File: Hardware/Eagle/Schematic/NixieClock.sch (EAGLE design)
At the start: 12 parts, among them X1 5566-12, X7 5566-12

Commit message: Made schematic a lot cleaner... pins routed from 2 driver chips to 1 SR
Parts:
- removed U$3, U$4: SN74HC595NDIP-16, SN74HC595N:SN74HC595NDIP-16
- removed U$5, U$6, U$7, U$8: DM5441ADIP-16, DM5441A:DM5441ADIP-16
- removed X7: 5566-12, con-molex:5566-12
- added X2: 5566-12, con-molex:5566-12
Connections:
- removed net N$29: U$3.QB, U$7.IN_C
- removed net N$30: U$4.QB, U$5.IN_C
- removed net N$31: U$4.QA, U$5.IN_D
- removed net N$32: U$3.QA, U$7.IN_D
- removed net N$33: U$5.OUT_0, X7-1.S
- removed net N$34: U$5.OUT_1, X7-2.S
- removed net N$35: U$5.OUT_2, X7-3.S
- removed net N$36: U$5.OUT_4, X7-5.S
- removed net N$37: U$5.OUT_5, X7-6.S
- removed net N$38: U$5.OUT_6, X7-7.S
- removed net N$39: U$5.OUT_7, X7-8.S
- removed net N$40: U$5.OUT_3, X7-4.S
- removed net N$41: U$5.OUT_8, X7-9.S
- removed net N$42: U$5.OUT_9, X7-10.S
- removed net N$43: U$10.OUT_0, X1-1.S
- removed net N$44: U$10.OUT_1, X1-2.S
- removed net N$45: X1-3.S
- removed net N$46: U$10.OUT_6, X1-7.S
- removed net N$47: U$10.OUT_7, X1-8.S
- removed net N$48: U$10.OUT_3, X1-4.S
- removed net N$49: U$10.OUT_4, X1-5.S
- removed net N$50: U$10.OUT_5, X1-6.S
- removed net N$51: X1-9.S
- removed net N$52: X1-10.S
- net N$1: now also U$10.IN_A, U$2.QE; no longer U$1.GND@0, U$10.GND, U$2.GND, U$3.GND, U$4.GND, U$5.GND, U$6.GND, U$7.GND, U$8.GND, U$9.GND
- net N$10: now also U$9.OUT_2, X1-3.S; no longer U$10.IN_A, U$2.QH
- net N$11: now also U$9.OUT_8, X1-9.S; no longer U$3.QH, U$8.IN_A
- net N$12: now also U$9.OUT_6, X1-7.S; no longer U$4.QH, U$6.IN_A
- net N$13: now also U$9.OUT_9, X1-10.S; no longer U$10.IN_B, U$2.QG
- net N$14: now also U$9.OUT_3, X1-4.S; no longer U$3.QG, U$8.IN_B
- net N$15: now also U$9.OUT_7, X1-8.S; no longer U$4.QG, U$6.IN_B
- net N$16: now also U$9.OUT_4, X1-5.S; no longer U$10.IN_C, U$2.QF
- net N$17: now also U$9.OUT_5, X1-6.S; no longer U$3.QF, U$8.IN_C
- net N$18: now also U$9.OUT_1, X1-2.S; no longer U$4.QF, U$6.IN_C
- net N$19: now also U$9.OUT_0, X1-1.S; no longer U$10.IN_D, U$2.QE
- net N$2: now also U$10.IN_B, U$2.QF; no longer U$1.3V3@2, U$2.SRCLR, U$2.VCC, U$3.SRCLR, U$3.VCC, U$4.SRCLR, U$4.VCC
- net N$20: now also U$10.OUT_6, X2-7.S; no longer U$3.QE, U$8.IN_D
- net N$21: now also U$10.OUT_3, X2-4.S; no longer U$4.QE, U$6.IN_D
- net N$22: now also U$10.OUT_7, X2-8.S; no longer U$2.QD, U$9.IN_A
- net N$23: now also U$10.OUT_4, X2-5.S; no longer U$3.QD, U$7.IN_A
- net N$24: now also U$10.OUT_5, X2-6.S; no longer U$4.QD, U$5.IN_A
- net N$25: now also U$10.OUT_1, X2-2.S; no longer U$2.QC, U$9.IN_B
- net N$26: now also U$10.OUT_0, X2-1.S; no longer U$3.QC, U$7.IN_B
- net N$27: now also U$10.OUT_9, X2-10.S; no longer U$4.QC, U$5.IN_B
- net N$28: now also U$10.OUT_8, X2-9.S; no longer U$2.QB, U$9.IN_C
- net N$3: now also U$2.VCC; no longer U$1.D4, U$2.SER
- net N$4: now also U$10.IN_C, U$2.QG; no longer U$1.D2, U$2.SRCLK, U$3.SRCLK, U$4.SRCLK
- net N$5: now also U$10.IN_D, U$2.QH; no longer U$1.D3, U$2.RCLK, U$3.RCLK, U$4.RCLK
- net N$6: now also U$2.QA, U$9.IN_A; no longer U$1.GND@3, U$2.OE, U$3.OE, U$4.OE
- net N$7: now also U$2.QB, U$9.IN_B; no longer U$2.QH*, U$3.SER
- net N$8: now also U$2.QC, U$9.IN_C; no longer U$1.3V3@0, U$10.VCC, U$5.VCC, U$6.VCC, U$7.VCC, U$8.VCC, U$9.VCC
- net N$9: now also U$2.QD, U$9.IN_D; no longer U$3.QH*, U$4.SER
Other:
- moved on the sheet: U$1, X1-1, X1-10, X1-11, X1-12, X1-2, X1-3, X1-4, X1-5, X1-6, X1-7, X1-8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

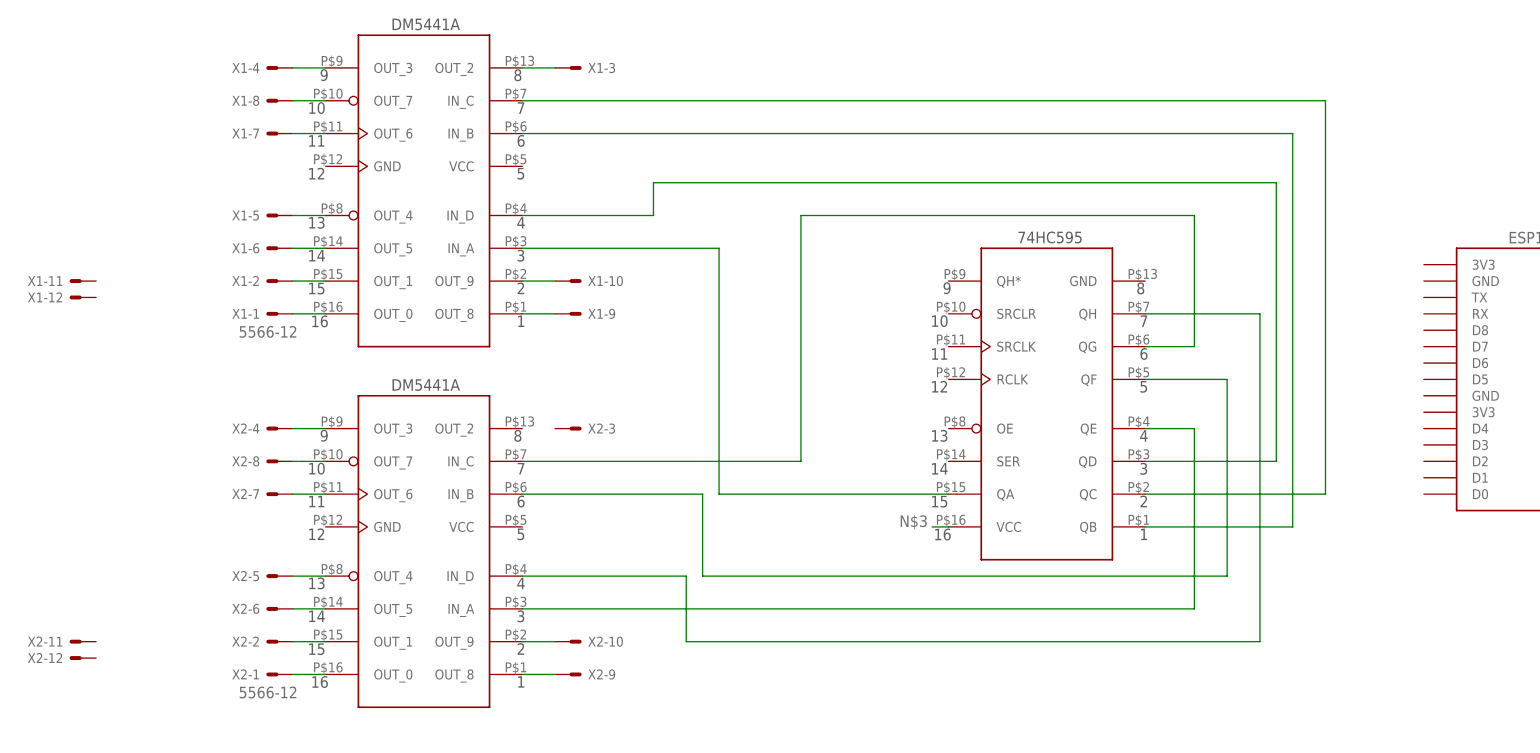
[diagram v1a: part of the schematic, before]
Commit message: 2 tubes routed
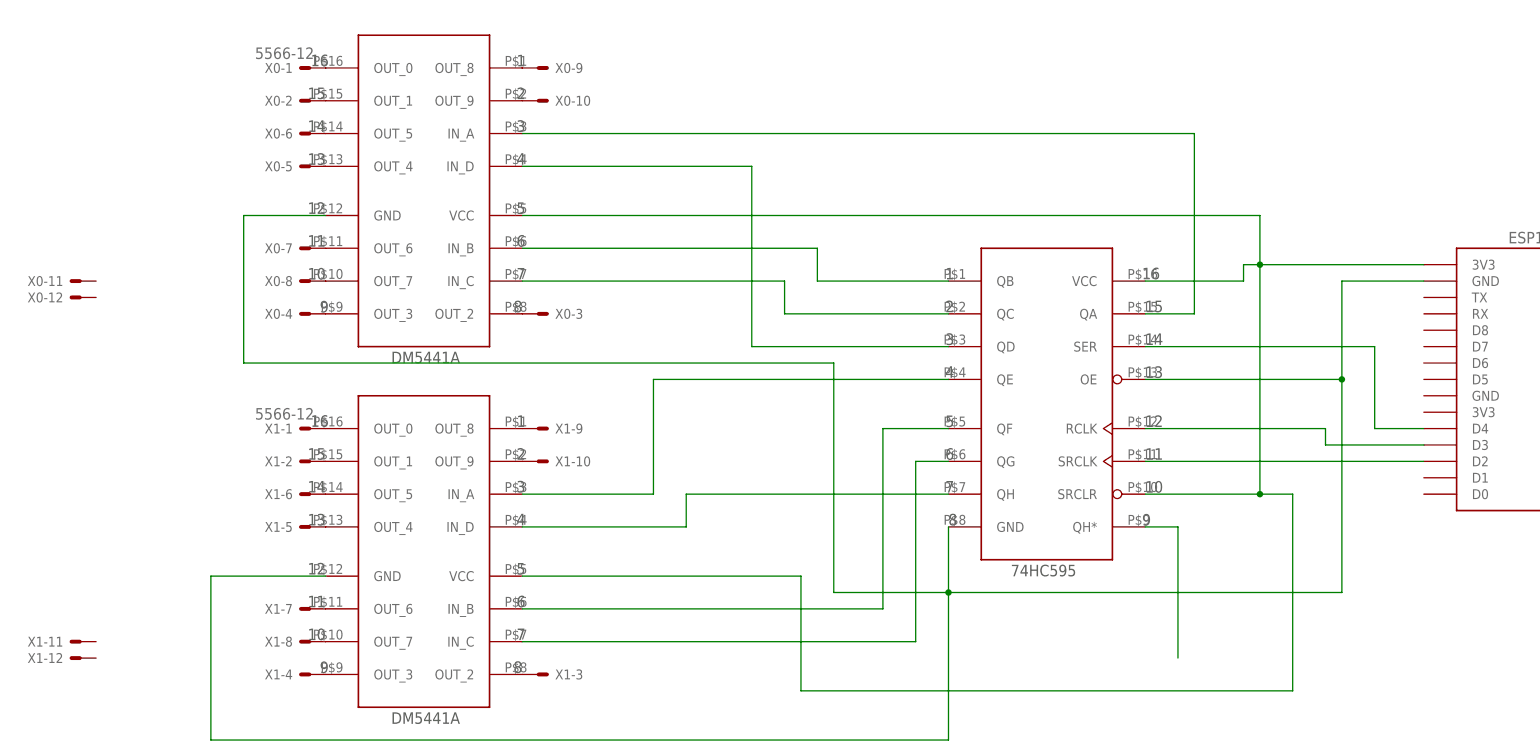
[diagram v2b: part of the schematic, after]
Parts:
- removed U$10, U$9: DM5441ADIP-16, DM5441A:DM5441ADIP-16
- removed U$2: SN74HC595NDIP-16, SN74HC595N:SN74HC595NDIP-16
- removed X2: 5566-12, con-molex:5566-12
- added BCD0, BCD1: DM5441ADIP-16, DM5441A:DM5441ADIP-16
- added SR0: SN74HC595NDIP-16, SN74HC595N:SN74HC595NDIP-16
- added X0: 5566-12, con-molex:5566-12
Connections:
- removed net N$1: U$10.IN_A, U$2.QE
- removed net N$25: U$10.OUT_1, X2-2.S
- removed net N$26: U$10.OUT_0, X2-1.S
- removed net N$28: U$10.OUT_8, X2-9.S
- new net N$30: BCD1.OUT_2, X1-3.S
- new net N$31: BCD1.OUT_6, X1-7.S
- new net N$32: BCD1.OUT_7, X1-8.S
- new net N$33: BCD1.OUT_3, X1-4.S
- new net N$34: BCD1.OUT_9, X1-10.S
- new net N$35: BCD1.OUT_8, X1-9.S
- new net N$36: BCD1.OUT_0, X1-1.S
- new net N$37: BCD1.OUT_1, X1-2.S
- new net N$38: BCD1.OUT_5, X1-6.S
- new net N$39: BCD1.OUT_4, X1-5.S
- net N$10: now also BCD1.IN_D, SR0.QH; no longer U$9.OUT_2, X1-3.S
- net N$11: now also SR0.SER, U$1.D4; no longer U$9.OUT_8, X1-9.S
- net N$12: now also BCD0.OUT_2, X0-3.S; no longer U$9.OUT_6, X1-7.S
- net N$13: now also SR0.RCLK, U$1.D3; no longer U$9.OUT_9, X1-10.S
- net N$14: now also BCD0.OUT_6, X0-7.S; no longer U$9.OUT_3, X1-4.S
- net N$15: now also BCD0.OUT_7, X0-8.S; no longer U$9.OUT_7, X1-8.S
- net N$16: now also BCD0.OUT_3, X0-4.S; no longer U$9.OUT_4, X1-5.S
- net N$17: now also BCD0.OUT_9, X0-10.S; no longer U$9.OUT_5, X1-6.S
- net N$18: now also BCD0.OUT_8, X0-9.S; no longer U$9.OUT_1, X1-2.S
- net N$19: now also BCD0.OUT_0, X0-1.S; no longer U$9.OUT_0, X1-1.S
- net N$2: now also BCD0.VCC, BCD1.VCC, SR0.SRCLR, SR0.VCC, U$1.3V3@2; no longer U$10.IN_B, U$2.QF
- net N$20: now also BCD0.OUT_1, X0-2.S; no longer U$10.OUT_6, X2-7.S
- net N$21: now also BCD0.OUT_5, X0-6.S; no longer U$10.OUT_3, X2-4.S
- net N$22: now also BCD0.OUT_4, X0-5.S; no longer U$10.OUT_7, X2-8.S
- net N$23: now also SR0.SRCLK, U$1.D2; no longer U$10.OUT_4, X2-5.S
- net N$24: now also BCD0.GND, BCD1.GND, SR0.GND, SR0.OE, U$1.GND@3; no longer U$10.OUT_5, X2-6.S
- net N$27: now also SR0.QH*; no longer U$10.OUT_9, X2-10.S
- net N$3: now also BCD0.IN_A, SR0.QA; no longer U$2.VCC
- net N$4: now also BCD0.IN_B, SR0.QB; no longer U$10.IN_C, U$2.QG
- net N$5: now also BCD0.IN_C, SR0.QC; no longer U$10.IN_D, U$2.QH
- net N$6: now also BCD0.IN_D, SR0.QD; no longer U$2.QA, U$9.IN_A
- net N$7: now also BCD1.IN_A, SR0.QE; no longer U$2.QB, U$9.IN_B
- net N$8: now also BCD1.IN_B, SR0.QF; no longer U$2.QC, U$9.IN_C
- net N$9: now also BCD1.IN_C, SR0.QG; no longer U$2.QD, U$9.IN_D
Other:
- moved on the sheet: X1-1, X1-10, X1-11, X1-12, X1-2, X1-3, X1-4, X1-5, X1-6, X1-7, X1-8, X1-9

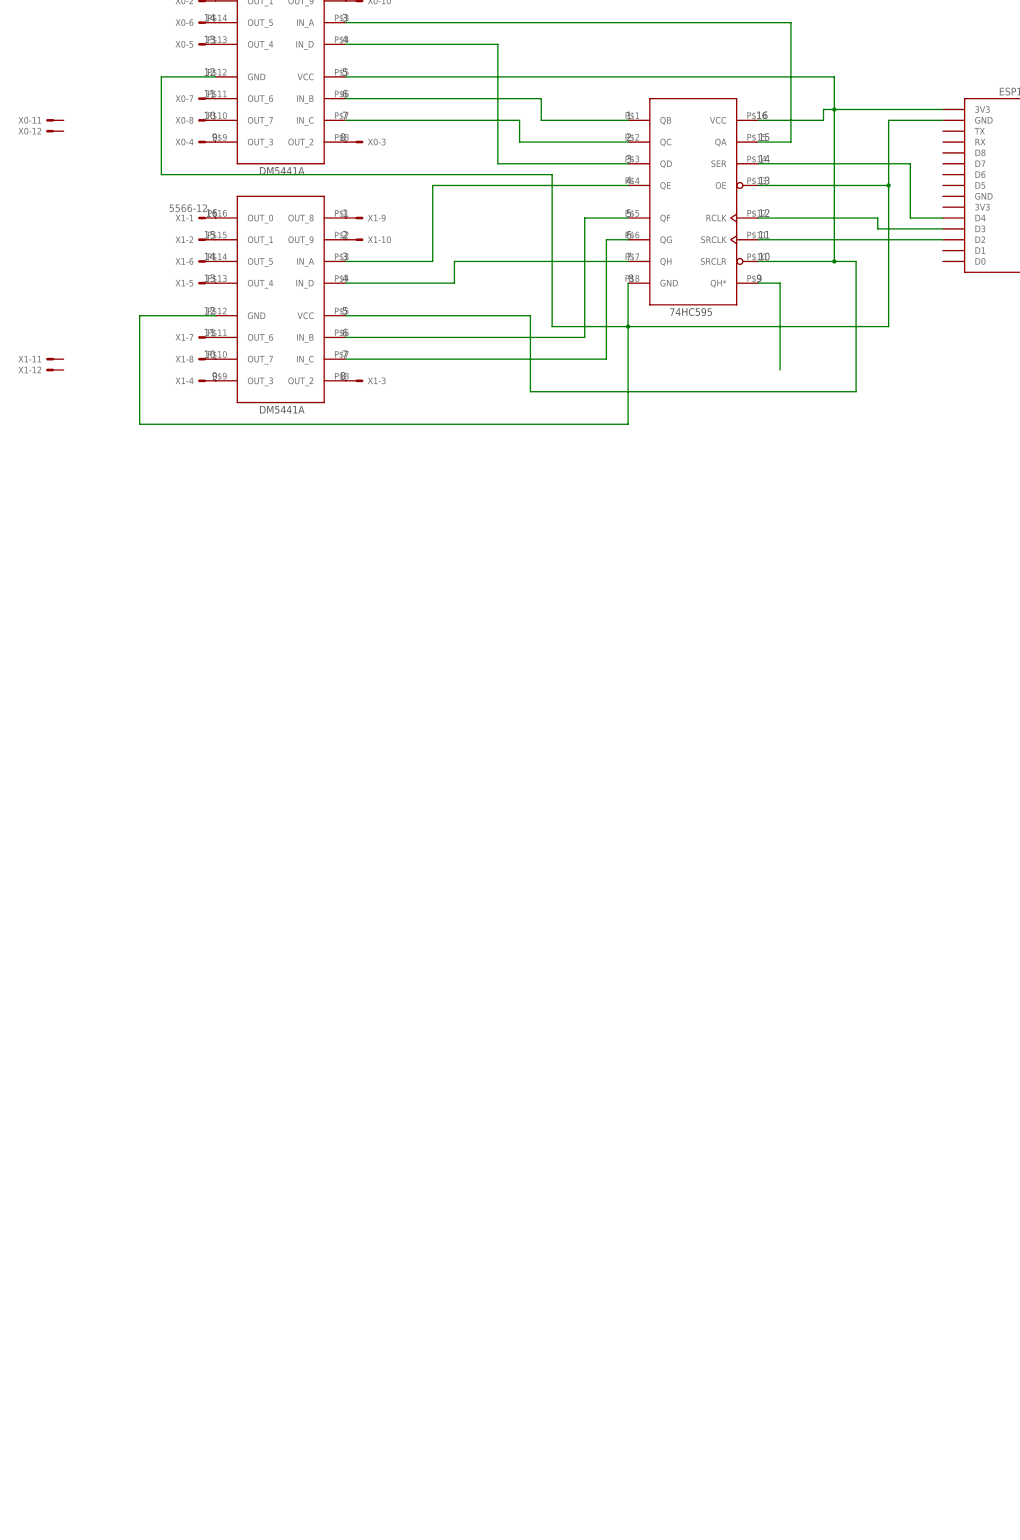
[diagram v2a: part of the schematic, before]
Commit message: Added all chips to schematic
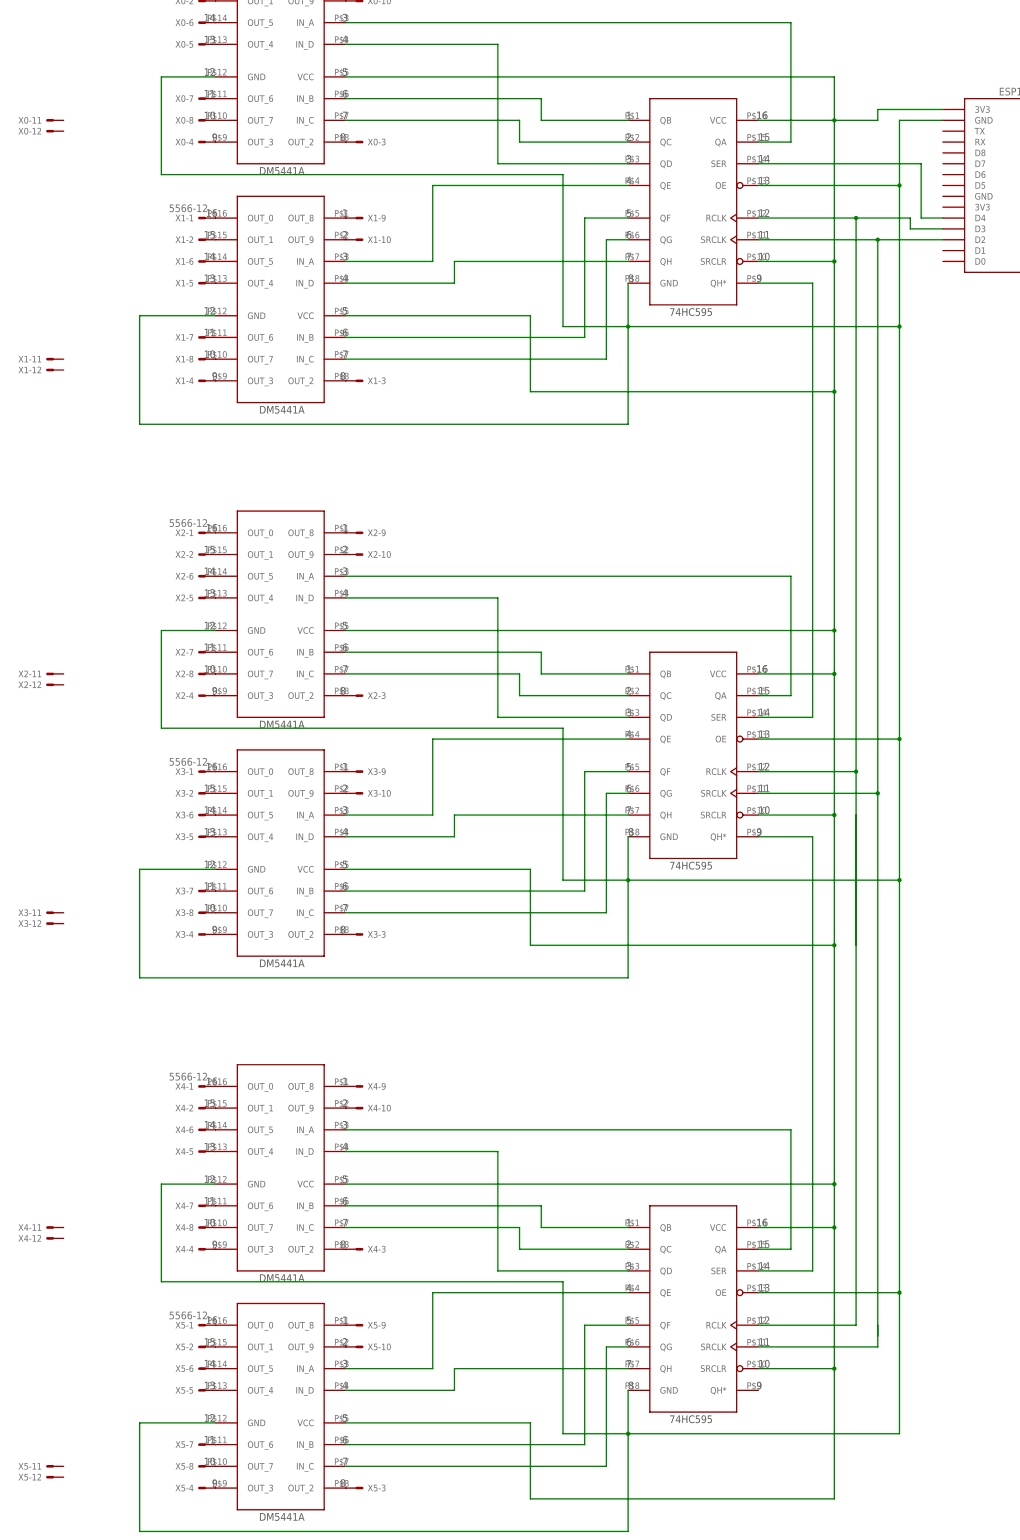
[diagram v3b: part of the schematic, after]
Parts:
- added BCD2, BCD3, BCD4, BCD5: DM5441ADIP-16, DM5441A:DM5441ADIP-16
- added SR1, SR2: SN74HC595NDIP-16, SN74HC595N:SN74HC595NDIP-16
- added X2, X3, X4, X5: 5566-12, con-molex:5566-12
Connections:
- removed net N$2: BCD0.VCC, BCD1.VCC, SR0.SRCLR, SR0.VCC, U$1.3V3@2
- removed net N$24: BCD0.GND, BCD1.GND, SR0.GND, SR0.OE, U$1.GND@3
- new net N$1: BCD2.IN_A, SR1.QA
- new net N$100: BCD5.OUT_5, X5-6.S
- new net N$101: BCD5.OUT_4, X5-5.S
- new net N$25: BCD2.IN_B, SR1.QB
- new net N$26: BCD2.IN_C, SR1.QC
- new net N$28: BCD2.IN_D, SR1.QD
- new net N$29: BCD3.IN_A, SR1.QE
- new net N$40: BCD3.IN_B, SR1.QF
- new net N$41: BCD3.IN_C, SR1.QG
- new net N$42: BCD3.IN_D, SR1.QH
- new net N$43: SR0.SRCLK, SR1.SRCLK, SR2.SRCLK, U$1.D2
- new net N$46: SR1.QH*, SR2.SER
- new net N$47: BCD2.OUT_2, X2-3.S
- new net N$48: BCD2.OUT_6, X2-7.S
- new net N$49: BCD2.OUT_7, X2-8.S
- new net N$50: BCD2.OUT_3, X2-4.S
- new net N$51: BCD2.OUT_9, X2-10.S
- new net N$52: BCD2.OUT_8, X2-9.S
- new net N$53: BCD2.OUT_0, X2-1.S
- new net N$54: BCD2.OUT_1, X2-2.S
- new net N$55: BCD2.OUT_5, X2-6.S
- new net N$56: BCD2.OUT_4, X2-5.S
- new net N$58: BCD3.OUT_2, X3-3.S
- new net N$59: BCD3.OUT_6, X3-7.S
- new net N$60: BCD3.OUT_7, X3-8.S
- new net N$61: BCD3.OUT_3, X3-4.S
- new net N$62: BCD3.OUT_9, X3-10.S
- new net N$63: BCD3.OUT_8, X3-9.S
- new net N$64: BCD3.OUT_0, X3-1.S
- new net N$65: BCD3.OUT_1, X3-2.S
- new net N$66: BCD3.OUT_5, X3-6.S
- new net N$67: BCD3.OUT_4, X3-5.S
- new net N$69: BCD4.IN_A, SR2.QA
- new net N$70: BCD4.IN_B, SR2.QB
- new net N$71: BCD4.IN_C, SR2.QC
- new net N$72: BCD4.IN_D, SR2.QD
- new net N$73: BCD5.IN_A, SR2.QE
- new net N$74: BCD5.IN_B, SR2.QF
- new net N$75: BCD5.IN_C, SR2.QG
- new net N$76: BCD5.IN_D, SR2.QH
- new net N$78: SR0.RCLK, SR1.RCLK, SR2.RCLK, U$1.D3
- new net N$81: BCD4.OUT_2, X4-3.S
- new net N$82: BCD4.OUT_6, X4-7.S
- new net N$83: BCD4.OUT_7, X4-8.S
- new net N$84: BCD4.OUT_3, X4-4.S
- new net N$85: BCD4.OUT_9, X4-10.S
- new net N$86: BCD4.OUT_8, X4-9.S
- new net N$87: BCD4.OUT_0, X4-1.S
- new net N$88: BCD4.OUT_1, X4-2.S
- new net N$89: BCD4.OUT_5, X4-6.S
- new net N$90: BCD4.OUT_4, X4-5.S
- new net N$92: BCD5.OUT_2, X5-3.S
- new net N$93: BCD5.OUT_6, X5-7.S
- new net N$94: BCD5.OUT_7, X5-8.S
- new net N$95: BCD5.OUT_3, X5-4.S
- new net N$96: BCD5.OUT_9, X5-10.S
- new net N$97: BCD5.OUT_8, X5-9.S
- new net N$98: BCD5.OUT_0, X5-1.S
- new net N$99: BCD5.OUT_1, X5-2.S
- net N$13: now also BCD0.VCC, BCD1.VCC, BCD2.VCC, BCD3.VCC, BCD4.VCC, BCD5.VCC, SR0.SRCLR, SR0.VCC, SR1.SRCLR, SR1.VCC, SR2.SRCLR, SR2.VCC, U$1.3V3@2; no longer SR0.RCLK, U$1.D3
- net N$23: now also BCD0.GND, BCD1.GND, BCD2.GND, BCD3.GND, BCD4.GND, BCD5.GND, SR0.GND, SR0.OE, SR1.GND, SR1.OE, SR2.GND, SR2.OE, U$1.GND@3; no longer SR0.SRCLK, U$1.D2
- net N$27: now also SR1.SER
